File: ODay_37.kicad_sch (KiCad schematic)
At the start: 11 parts, among them SW1 Rotary Battery Select (Only u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, U1 Renogy BC50D1S Solar Controll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, U2 Dual_10A_Battery_Charger

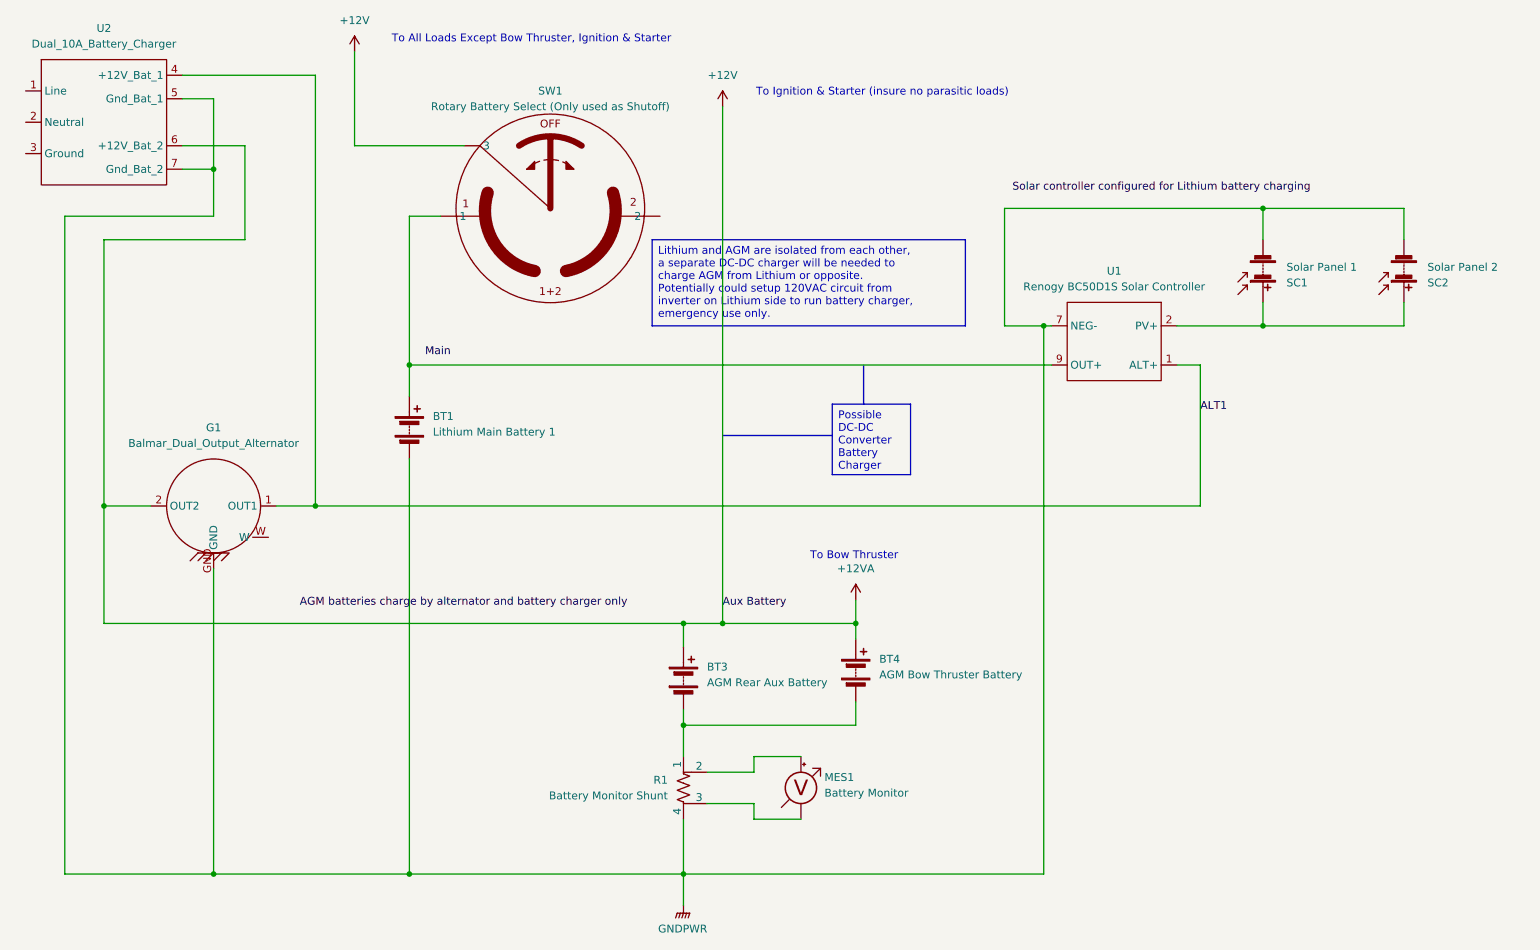
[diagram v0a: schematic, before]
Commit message: Add dedicated lithium charger and IGN input to solar ctrlr
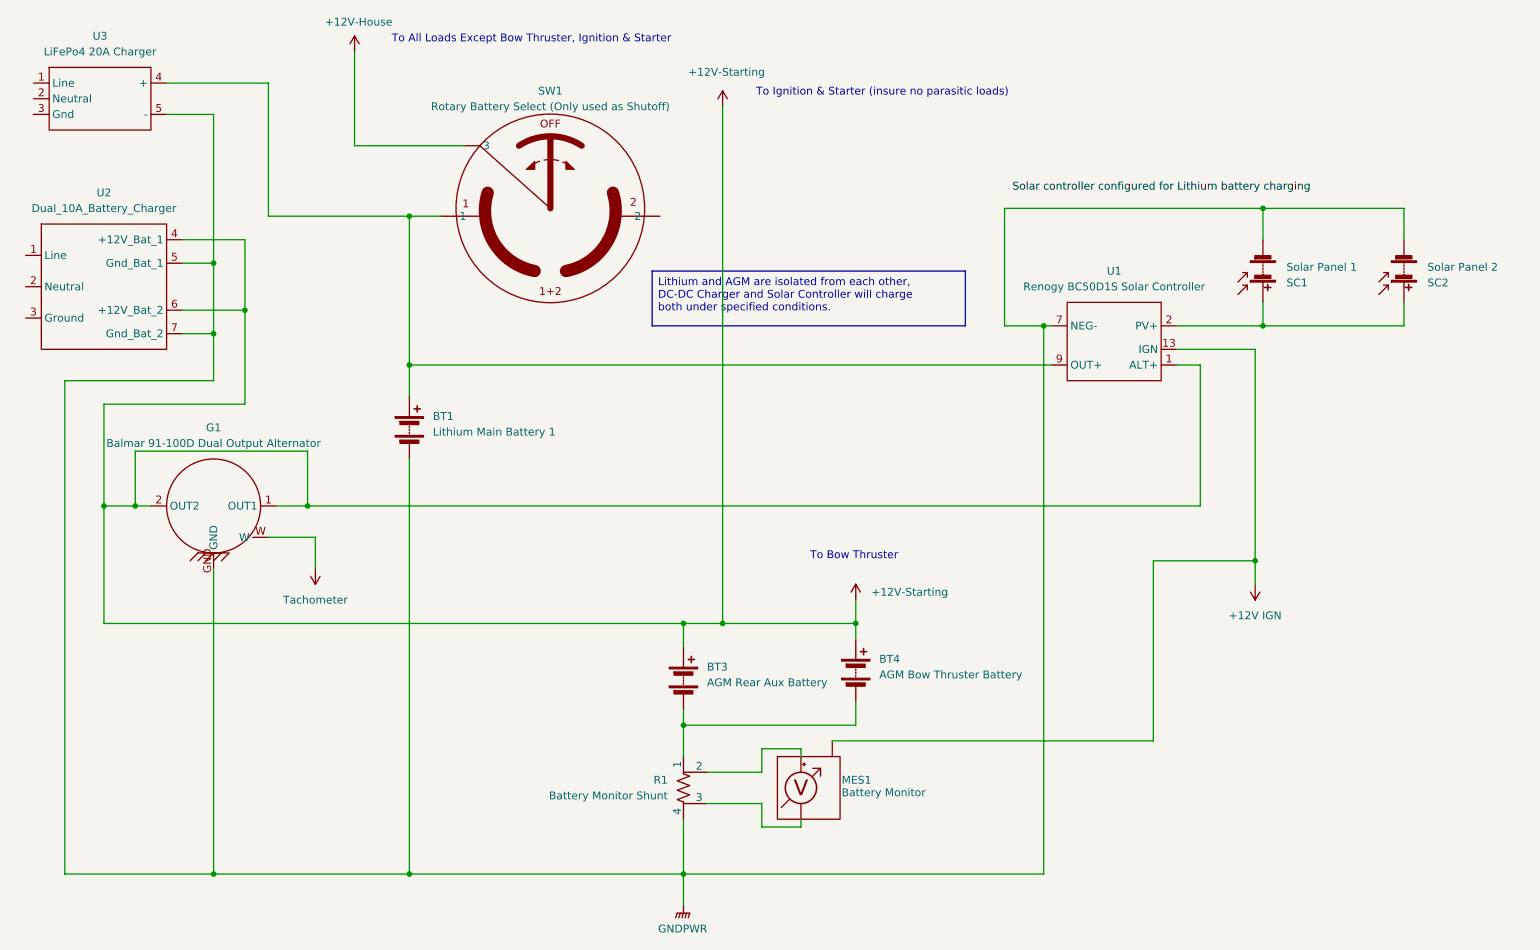
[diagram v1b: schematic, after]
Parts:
- added U3: LiFePo4 20A Charger, symbol Battery_Charger:LiFePo4 20A Charger
- G1: value Balmar_Dual_Output_Alternator -> Balmar 91-100D Dual Output Alternator
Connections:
- net ALT1 is gone; now on net +12V-Starting: G1.1 (OUT1), U1.1 (ALT+), U2.4 (+12V_Bat_1)
- net GNDPWR: now also U3.5 (-)
- net at BT1.1 (+), SW1. (2), U1.9 (OUT+): now also U3.4 (+)
- net +12V-House: now reaches SW1. (2)
- net Tachometer: now reaches G1.W
- net +12V renamed +12V-Starting
- net +12V-Starting: no longer SW1. (2)
- new net +12V IGN: MES1.3 (Pwr), U1.13 (IGN)
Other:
- moved on the sheet: U2
